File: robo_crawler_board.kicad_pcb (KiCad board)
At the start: 2 copper layers, 108.2 x 91 mm, 24 parts, among them J1 Screw_Terminal_01x02, J2 Screw_Terminal_01x02, J3 Screw_Terminal_01x02, J4 Screw_Terminal_01x02, J5 Screw_Terminal_01x02, J6 Screw_Terminal_01x02, J7 Screw_Terminal_01x02, J8 Screw_Terminal_01x02, J9 Screw_Terminal_01x02, Q1 IRLZ44N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

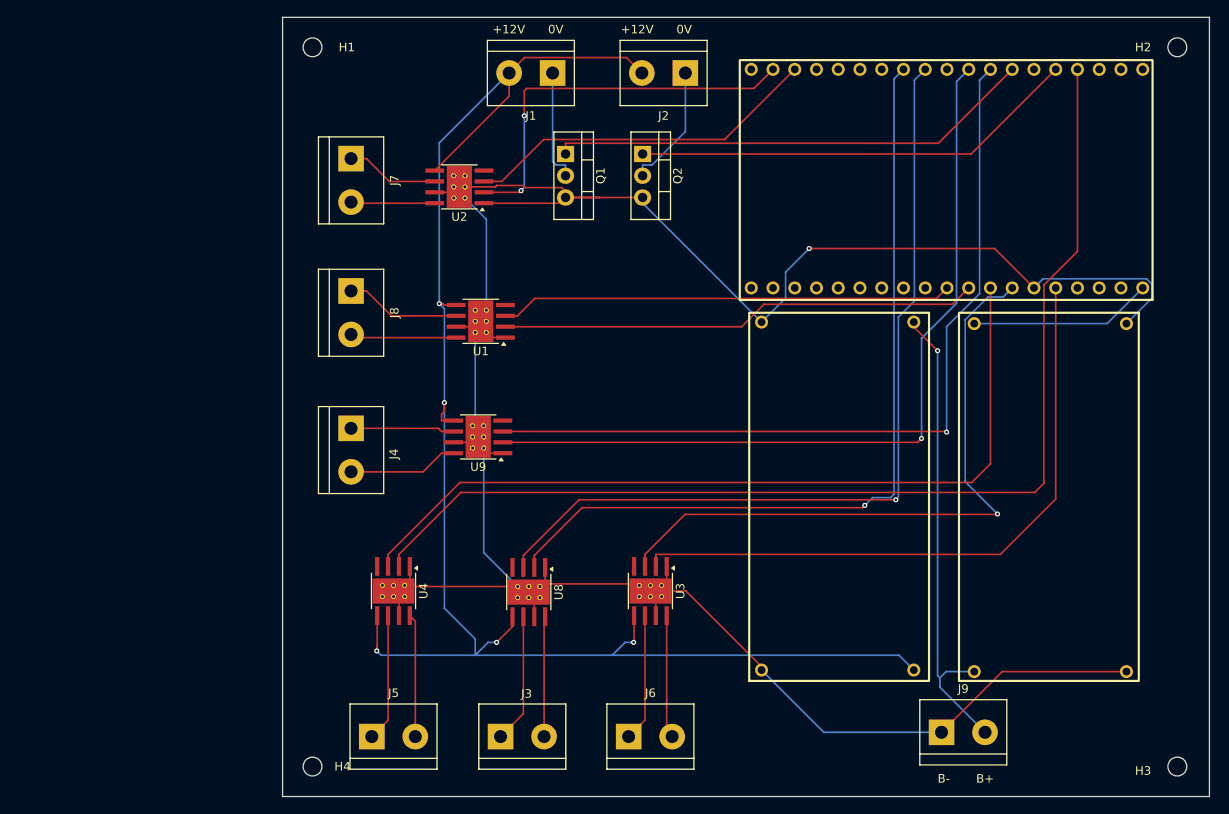
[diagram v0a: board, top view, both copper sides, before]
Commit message: adjusted for EPL manufacturing
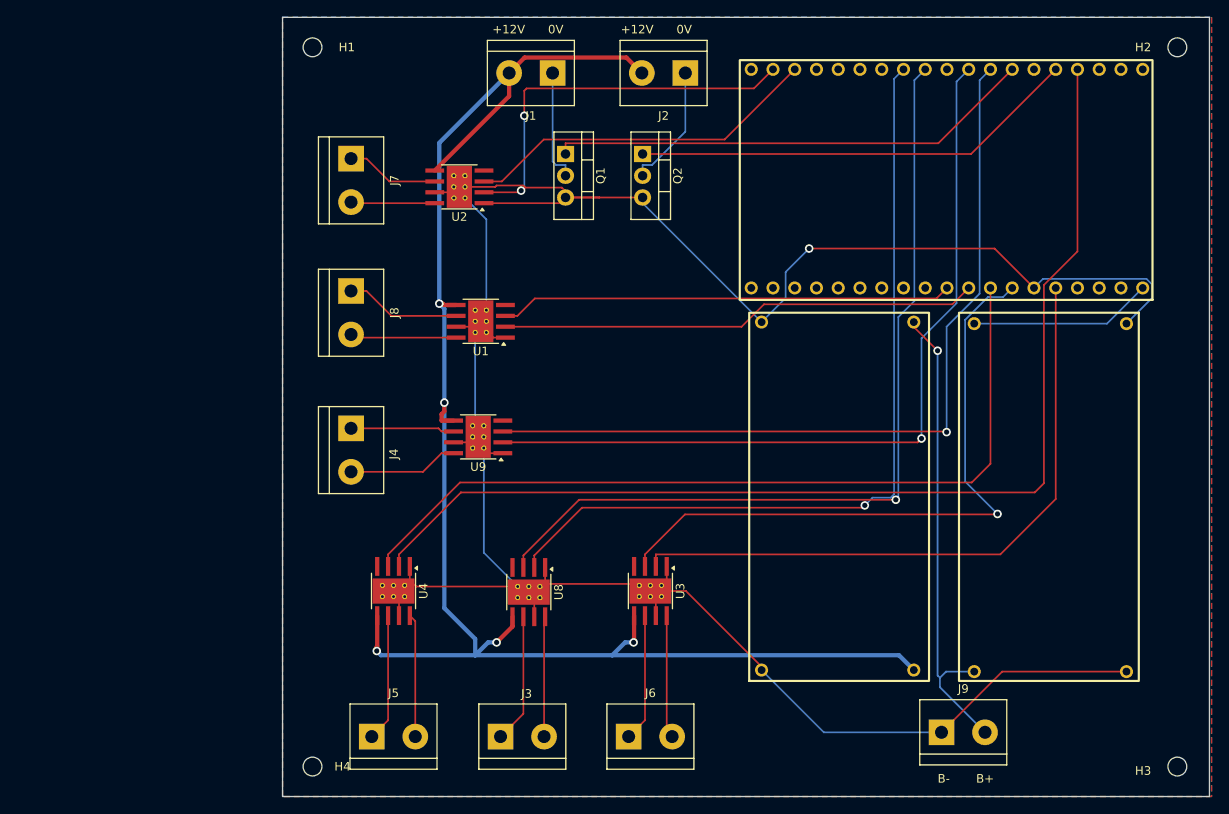
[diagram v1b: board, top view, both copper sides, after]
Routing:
- added copper zone on B.Cu, net GND
- added copper zone on F.Cu, net GND
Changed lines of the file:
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@@
 		(tenting front back)
 		(pcbplotparams
-			(layerselection 0x00000000_00000000_55555555_5755f5ff)
+			(layerselection 0x00000000_00000000_55555555_57555555)
 			(plot_on_all_layers_selection 0x00000000_00000000_00000000_00000000)
 			(disableapertmacros no)
@@
 			(outputformat 1)
 			(mirror no)
-			(drillshape 1)
+			(drillshape 0)
 			(scaleselection 1)
 			(outputdirectory "")
@@
 		(start 190.9635 125.4715)
 		(end 190.722 125.23)
-		(width 0.2)
+		(width 0.5)
 		(layer "F.Cu")
 		(net 2)
@@
 		(start 135.8968 95.0168)
 		(end 135.5733 95.3403)
-		(width 0.2)
+		(width 0.5)
 		(layer "F.Cu")
 		(net 2)
@@
 		(start 143.46 55.5)
 		(end 143.46 58.21)
-		(width 0.2)
+		(width 0.5)
 		(layer "F.Cu")
 		(net 2)
@@
 		(start 128 123)
 		(end 128 122.5)
-		(width 0.2)
+		(width 0.5)
 		(layer "F.Cu")
 		(net 2)
@@
 		(start 135.5733 95.3403)
 		(end 135.5733 96.095)
-		(width 0.2)
+		(width 0.5)
 		(layer "F.Cu")
 		(net 2)
@@
 		(start 145.2617 53.6983)
 		(end 157.1583 53.6983)
-		(width 0.2)
+		(width 0.5)
 		(layer "F.Cu")
 		(net 2)
@@
 		(start 135.3027 82.4375)
 		(end 135.7158 82.4375)
-		(width 0.2)
+		(width 0.5)
 		(layer "F.Cu")
 		(net 2)
@@
 		(start 135.5733 96.095)
 		(end 136.975 96.095)
-		(width 0.2)
+		(width 0.5)
 		(layer "F.Cu")
 		(net 2)
@@
 		(start 142 122)
 		(end 143.855 120.145)
-		(width 0.2)
+		(width 0.5)
 		(layer "F.Cu")
 		(net 2)
@@
 		(start 158.055 121.945)
 		(end 158.055 118.875)
-		(width 0.2)
+		(width 0.5)
 		(layer "F.Cu")
 		(net 2)
@@
 		(start 143.46 55.5)
 		(end 145.2617 53.6983)
-		(width 0.2)
+		(width 0.5)
 		(layer "F.Cu")
 		(net 2)
@@
 		(start 158 122)
 		(end 158.055 121.945)
-		(width 0.2)
+		(width 0.5)
 		(layer "F.Cu")
 		(net 2)
@@
 		(start 143.855 120.145)
 		(end 143.855 119)
-		(width 0.2)
+		(width 0.5)
 		(layer "F.Cu")
 		(net 2)
@@
 		(start 135.8733 82.595)
 		(end 137.275 82.595)
-		(width 0.2)
+		(width 0.5)
 		(layer "F.Cu")
 		(net 2)
@@
 		(start 128 122.5)
 		(end 128.055 122.445)
-		(width 0.2)
+		(width 0.5)
 		(layer "F.Cu")
 		(net 2)
@@
 		(start 128.055 122.445)
 		(end 128.055 118.875)
-		(width 0.2)
+		(width 0.5)
 		(layer "F.Cu")
 		(net 2)
@@
 		(start 157.1583 53.6983)
 		(end 158.96 55.5)
-		(width 0.2)
+		(width 0.5)
 		(layer "F.Cu")
 		(net 2)
@@
 		(start 143.46 58.21)
 		(end 134.775 66.895)
-		(width 0.2)
+		(width 0.5)
 		(layer "F.Cu")
 		(net 2)
@@
 		(start 135.7158 82.4375)
 		(end 135.8733 82.595)
-		(width 0.2)
+		(width 0.5)
 		(layer "F.Cu")
 		(net 2)
@@
 		(start 135.8968 94)
 		(end 135.8968 95.0168)
-		(width 0.2)
+		(width 0.5)
 		(layer "F.Cu")
 		(net 2)
@@
 	(via
 		(at 128 123)
-		(size 0.6)
-		(drill 0.3)
+		(size 1)
+		(drill 0.6)
 		(layers "F.Cu" "B.Cu")
 		(net 2)
@@
 	(via
 		(at 135.8968 94)
-		(size 0.6)
-		(drill 0.3)
+		(size 1)
+		(drill 0.6)
 		(layers "F.Cu" "B.Cu")
 		(net 2)
@@
 	(via
 		(at 142 122)
-		(size 0.6)
-		(drill 0.3)
+		(size 1)
+		(drill 0.6)
 		(layers "F.Cu" "B.Cu")
 		(net 2)
@@
 	(via
 		(at 135.3027 82.4375)
-		(size 0.6)
-		(drill 0.3)
+		(size 1)
+		(drill 0.6)
 		(layers "F.Cu" "B.Cu")
 		(net 2)
@@
 	(via
 		(at 158 122)
-		(size 0.6)
-		(drill 0.3)
+		(size 1)
+		(drill 0.6)
 		(layers "F.Cu" "B.Cu")
 		(net 2)
@@
 		(start 190.722 125.23)
 		(end 188.992 123.5)
-		(width 0.2)
+		(width 0.5)
 		(layer "B.Cu")
 		(net 2)
@@
 		(start 188.992 123.5)
 		(end 155.5 123.5)
-		(width 0.2)
+		(width 0.5)
 		(layer "B.Cu")
 		(net 2)
@@
 		(start 128.5 123.5)
 		(end 128 123)
-		(width 0.2)
+		(width 0.5)
 		(layer "B.Cu")
 		(net 2)
@@
 		(start 155.5 123.5)
 		(end 157 122)
-		(width 0.2)
+		(width 0.5)
 		(layer "B.Cu")
 		(net 2)
@@
 		(start 135.3027 82.4375)
 		(end 135.3027 63.6573)
-		(width 0.2)
+		(width 0.5)
 		(layer "B.Cu")
 		(net 2)
@@
 		(start 141 122)
 		(end 142 122)
-		(width 0.2)
+		(width 0.5)
 		(layer "B.Cu")
 		(net 2)
@@
 		(start 139.5 123.5)
 		(end 141 122)
-		(width 0.2)
+		(width 0.5)
 		(layer "B.Cu")
 		(net 2)
@@
 		(start 135.8968 94)
 		(end 135.8968 118)
-		(width 0.2)
+		(width 0.5)
 		(layer "B.Cu")
 		(net 2)
@@
 		(start 135.8968 94)
 		(end 135.8968 83.0316)
-		(width 0.2)
+		(width 0.5)
 		(layer "B.Cu")
 		(net 2)
@@
 		(start 139.5 121.6032)
 		(end 135.8968 118)
-		(width 0.2)
+		(width 0.5)
 		(layer "B.Cu")
 		(net 2)
@@
 		(start 139.5 123.5)
 		(end 128.5 123.5)
-		(width 0.2)
+		(width 0.5)
 		(layer "B.Cu")
 		(net 2)
@@
 		(start 157 122)
 		(end 158 122)
-		(width 0.2)
+		(width 0.5)
 		(layer "B.Cu")
 		(net 2)
@@
 		(start 135.3027 63.6573)
 		(end 143.46 55.5)
-		(width 0.2)
+		(width 0.5)
 		(layer "B.Cu")
 		(net 2)
@@
 		(start 135.8968 83.0316)
 		(end 135.3027 82.4375)
-		(width 0.2)
+		(width 0.5)
 		(layer "B.Cu")
 		(net 2)
@@
 		(start 155.5 123.5)
 		(end 139.5 123.5)
-		(width 0.2)
+		(width 0.5)
 		(layer "B.Cu")
 		(net 2)
@@
 		(start 139.5 123.5)
 		(end 139.5 121.6032)
-		(width 0.2)
+		(width 0.5)
 		(layer "B.Cu")
 		(net 2)
@@
 	(via
 		(at 178.5 76)
-		(size 0.6)
-		(drill 0.3)
+		(size 1)
+		(drill 0.6)
 		(layers "F.Cu" "B.Cu")
 		(net 16)
@@
 	(via
 		(at 145.2315 60.5)
-		(size 0.6)
-		(drill 0.3)
+		(size 1)
+		(drill 0.6)
 		(layers "F.Cu" "B.Cu")
 		(net 23)
@@
 	(via
 		(at 144.861 69.2384)
-		(size 0.6)
-		(drill 0.3)
+		(size 1)
+		(drill 0.6)
 		(layers "F.Cu" "B.Cu")
 		(net 23)
@@
 	(via
 		(at 200.5 107)
-		(size 0.6)
-		(drill 0.3)
+		(size 1)
+		(drill 0.6)
 		(layers "F.Cu" "B.Cu")
 		(net 27)
@@
 	(via
 		(at 188.6216 105.3433)
-		(size 0.6)
-		(drill 0.3)
+		(size 1)
+		(drill 0.6)
 		(layers "F.Cu" "B.Cu")
 		(net 36)
@@
 	(via
 		(at 185 106)
-		(size 0.6)
-		(drill 0.3)
+		(size 1)
+		(drill 0.6)
 		(layers "F.Cu" "B.Cu")
 		(net 48)
@@
 	(via
 		(at 191.6219 98.1885)
-		(size 0.6)
-		(drill 0.3)
+		(size 1)
+		(drill 0.6)
 		(layers "F.Cu" "B.Cu")
 		(net 50)
@@
 	(via
 		(at 194.5548 97.441)
-		(size 0.6)
-		(drill 0.3)
+		(size 1)
+		(drill 0.6)
 		(layers "F.Cu" "B.Cu")
 		(net 55)
@@
 	(via
 		(at 193.5 87.9351)
-		(size 0.6)
-		(drill 0.3)
+		(size 1)
+		(drill 0.6)
 		(layers "F.Cu" "B.Cu")
 		(net 60)
@@
 		(net 60)
 	)
+	(zone
+		(net 16)
+		(net_name "GND")
+		(layers "F.Cu" "B.Cu")
+		(hatch edge 0.5)
+		(connect_pads
+			(clearance 0.5)
+		)
+		(min_thickness 0.25)
+		(filled_areas_thickness no)
+		(fill yes
+			(thermal_gap 0.5)
+			(thermal_bridge_width 0.5)
+		)
+		(polygon
+			(pts
+				(xy 117 49) (xy 225.5 49) (xy 225.5 140) (xy 117 140)
+			)
+		)
+	)
 	(embedded_fonts no)

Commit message: cleaning repo
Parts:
- added R1: 15k, Resistor_SMD:R_0805_2012Metric, F.Cu at (144.1, 79.5)
- added R2: 15k, Resistor_SMD:R_0805_2012Metric, F.Cu at (141.1, 64.5)
- added R3: 15k, Resistor_SMD:R_0805_2012Metric, F.Cu at (154.9, 113.0)
- added R4: 15k, Resistor_SMD:R_0805_2012Metric, F.Cu at (124.5, 114.1)
- added R5: 15k, Resistor_SMD:R_0805_2012Metric, F.Cu at (139.9, 113.0)
- added R6: 15k, Resistor_SMD:R_0805_2012Metric, F.Cu at (142.0, 93.0)
- H1, H2, H3, H4: value M2 Size -> MountingHole
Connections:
- U1 pad 4: unconnected-(U1-ILIM-Pad4) -> Net-(U1-ILIM)
- U2 pad 4: unconnected-(U2-ILIM-Pad4) -> Net-(U2-ILIM)
- U3 pad 4: unconnected-(U3-ILIM-Pad4) -> Net-(U3-ILIM)
- U4 pad 4: unconnected-(U4-ILIM-Pad4) -> Net-(U4-ILIM)
- U8 pad 4: unconnected-(U8-ILIM-Pad4) -> Net-(U8-ILIM)
- U9 pad 4: unconnected-(U9-ILIM-Pad4) -> Net-(U9-ILIM)
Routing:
- net GND: track 316.8 -> 361.3 mm
- net +12V: track 192.1 -> 202.2 mm
- net Net-(U4-ILIM): track 0.00 -> 3.58 mm
- net Net-(U3-IN1): track 75.8 -> 72.3 mm
- net Net-(U9-ILIM): track 0.00 -> 3.17 mm
- net Net-(U1-ILIM): track 0.00 -> 3.16 mm
- net Net-(U8-ILIM): track 0.00 -> 3.13 mm
- net Net-(U2-ILIM): track 0.00 -> 2.54 mm
- net Net-(U2-IN2): track 47.4 -> 45.0 mm
- net Net-(U3-ILIM): track 0.00 -> 2.28 mm
- removed copper zone on B.Cu, net GND
- removed copper zone on F.Cu, net GND

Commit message: Reworking board design
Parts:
- removed J8, J9: Screw_Terminal_01x02, TerminalBlock:TerminalBlock_bornier-2_P5.08mm
- removed Q1, Q2: IRLZ44N, Package_TO_SOT_THT:TO-220-3_Vertical
- H1, H2, H4: footprint MountingHole:MountingHole_2.2mm_M2 -> MountingHole:MountingHole_2.2mm_M2_Pad
- H3: value MountingHole -> M2; footprint MountingHole:MountingHole_2.2mm_M2 -> MountingHole:MountingHole_2.2mm_M2_Pad
- U1: value DRV8871DDA -> ~; footprint Package_SO:Texas_HTSOP-8-1EP_3.9x4.9mm_P1.27mm_EP2.95x4.9mm_Mask2.4x3.1mm_ThermalVias -> deadzone_footprints:esp32-32u
- U2, U3: value DRV8871DDA -> ~; footprint Package_SO:Texas_HTSOP-8-1EP_3.9x4.9mm_P1.27mm_EP2.95x4.9mm_Mask2.4x3.1mm_ThermalVias -> deadzone_footprints:LM2596 DC-DC Buck Converter
- U5: value ~ -> DRV8871DDA; footprint deadzone_footprints:esp32-32u -> Package_SO:Texas_HTSOP-8-1EP_3.9x4.9mm_P1.27mm_EP2.95x4.9mm_Mask2.4x3.1mm_ThermalVias
- U6, U7: value ~ -> DRV8871DDA; footprint deadzone_footprints:LM2596 DC-DC Buck Converter -> Package_SO:Texas_HTSOP-8-1EP_3.9x4.9mm_P1.27mm_EP2.95x4.9mm_Mask2.4x3.1mm_ThermalVias
- moved U6 102.6 mm to (104.1, 99.4), turned to 180 degrees
- moved U5 91.5 mm to (103.8, 80.4)
- moved U7 82.3 mm to (100.0, 112.4), turned to 180 degrees
- moved J3 76.5 mm to (92.7, 74.9), turned to -90 degrees
- moved J2 61.5 mm to (102.5, 57.1)
- moved U4 57.2 mm to (99.8, 67.3), turned to 180 degrees
- moved J1 48.6 mm to (180.0, 92.5), turned to 90 degrees
- moved R3 41.8 mm to (116.0, 97.8), turned to 0 degrees
- moved H3 40.5 mm to (182.6, 125.0)
- moved H2 38.9 mm to (182.6, 54.5)
- moved J6 38.4 mm to (120.7, 121.9)
- moved R1 36.0 mm to (111.0, 65.2)
- moved U9 34.7 mm to (123.1, 67.7)
- moved H4 32.9 mm to (89.6, 125.0)
- moved J4 32.5 mm to (92.7, 100.3)
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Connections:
- J1 pad 2: +12V -> Net-(J1-Pin_2)
- J2 pad 2: +12V -> Net-(J2-Pin_2)
- R1 pad 1: Net-(U1-ILIM) -> Net-(U4-ILIM)
- R2 pad 1: Net-(U2-ILIM) -> Net-(U5-ILIM)
- R3 pad 1: Net-(U3-ILIM) -> Net-(U6-ILIM)
- R4 pad 1: Net-(U4-ILIM) -> Net-(U7-ILIM)
- U1 pad 1: GND -> +5V
- U1 pad 2: Net-(U1-IN2) -> unconnected-(U1-VDD33-Pad2)
- U1 pad 3: Net-(U1-IN1) -> unconnected-(U1-EN-Pad3)
- U1 pad 4: Net-(U1-ILIM) -> unconnected-(U1-VP-Pad4)
- U1 pad 5: +12V -> unconnected-(U1-VN-Pad5)
- U1 pad 6: Net-(J8-Pin_1) -> unconnected-(U1-IO34-Pad6)
- U1 pad 7: GND -> unconnected-(U1-IO35-Pad7)
- U1 pad 8: Net-(J8-Pin_2) -> unconnected-(U1-IO32-Pad8)
- U1 pad 9: GND -> unconnected-(U1-IO33-Pad9)
- U2 pad 1: GND -> Net-(J1-Pin_1)
- U2 pad 2: Net-(U2-IN2) -> Net-(J1-Pin_2)
- U2 pad 3: Net-(U2-IN1) -> GND
- U2 pad 4: Net-(U2-ILIM) -> +12V
- U3 pad 1: GND -> Net-(J1-Pin_1)
- U3 pad 2: Net-(U3-IN2) -> Net-(J1-Pin_2)
- U3 pad 3: Net-(U3-IN1) -> GND
- U3 pad 4: Net-(U3-ILIM) -> +5V
- U4 pad 2: Net-(U4-IN2) -> MOTOR1_CH2
- U4 pad 3: Net-(U4-IN1) -> MOTOR1_CH1
- U4 pad 6: Net-(J5-Pin_1) -> Net-(J2-Pin_1)
- U4 pad 8: Net-(J5-Pin_2) -> Net-(J2-Pin_2)
- U5 pad 1: +5V -> GND
- U5 pad 2: unconnected-(U5-VDD33-Pad2) -> MOTOR2_CH2
- U5 pad 3: unconnected-(U5-EN-Pad3) -> MOTOR2_CH1
- U5 pad 4: unconnected-(U5-VP-Pad4) -> Net-(U5-ILIM)
- U5 pad 5: unconnected-(U5-VN-Pad5) -> +12V
- U5 pad 6: unconnected-(U5-IO34-Pad6) -> Net-(J3-Pin_1)
- U5 pad 7: unconnected-(U5-IO35-Pad7) -> GND
- U5 pad 8: unconnected-(U5-IO32-Pad8) -> Net-(J3-Pin_2)
- U5 pad 9: unconnected-(U5-IO33-Pad9) -> GND
- U6 pad 2: /+Vin -> MOTOR3_CH2
- U6 pad 3: GND -> MOTOR3_CH1
- U6 pad 4: +5V -> Net-(U6-ILIM)
- U7 pad 2: /+Vin -> MOTOR4_CH2
- U7 pad 3: GND -> MOTOR4_CH1
- U7 pad 4: +12V -> Net-(U7-ILIM)
- U8 pad 2: Net-(U5-IO19) -> MOTOR5_CH2
- U8 pad 3: Net-(U5-IO18) -> MOTOR5_CH1
- U8 pad 6: Net-(J3-Pin_1) -> Net-(J6-Pin_1)
- U8 pad 8: Net-(J3-Pin_2) -> Net-(J6-Pin_2)
- U9 pad 2: Net-(U5-IO17) -> MOTOR6_CH2
- U9 pad 3: Net-(U5-IO16) -> MOTOR6_CH1
- U9 pad 6: Net-(J4-Pin_1) -> Net-(J7-Pin_1)
- U9 pad 8: Net-(J4-Pin_2) -> Net-(J7-Pin_2)
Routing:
- net GND: track 361.3 -> 0.00 mm, vias 1 -> 0
- net +12V: track 202.2 -> 0.00 mm, vias 5 -> 0
- net Net-(U4-IN2): track 130.1 -> 0.00 mm
- net Net-(U5-IO18): track 99.3 -> 0.00 mm, vias 1 -> 0
- net Net-(U5-IO16): track 96.8 -> 0.00 mm, vias 1 -> 0
- net Net-(U4-IN1): track 96.7 -> 0.00 mm
- net Net-(U5-IO19): track 96.1 -> 0.00 mm, vias 1 -> 0
- net Net-(U5-IO17): track 95.7 -> 0.00 mm, vias 1 -> 0
- net Net-(U3-IN2): track 75.4 -> 0.00 mm
- net Net-(U3-IN1): track 72.3 -> 0.00 mm, vias 1 -> 0
- net Net-(Q1-G): track 57.0 -> 0.00 mm
- net Net-(U1-IN2): track 56.0 -> 0.00 mm
- net /+Vin: track 55.5 -> 0.00 mm, vias 1 -> 0
- net Net-(U1-IN1): track 52.9 -> 0.00 mm
- net Net-(Q2-G): track 52.3 -> 0.00 mm
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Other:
- board outline removed
- board text removed: "+12V"
- board text removed: "0V"
- board text removed: "B+"
- board text removed: "B-"

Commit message: tentative rev2
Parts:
- H1, H2, H4: value MountingHole -> M2
- moved J5 0.58 mm to (97.8, 122.5)
- moved J6 0.58 mm to (120.7, 122.5)
- moved R1 0.56 mm to (110.5, 65.5)
- moved R3 0.29 mm to (116.0, 97.5)
- moved R2 0.24 mm to (116.0, 78.5)
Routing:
- net +12V: track 0.00 -> 135.4 mm, vias 0 -> 6
- net +5V: track 0.00 -> 117.0 mm
- net MOTOR4_CH2: track 0.00 -> 60.7 mm, vias 0 -> 1
- net GND: track 0.00 -> 59.3 mm, vias 0 -> 3
- net MOTOR5_CH2: track 0.00 -> 57.9 mm, vias 0 -> 1
- net Net-(J1-Pin_2): track 0.00 -> 57.8 mm
- net Net-(J1-Pin_1): track 0.00 -> 57.1 mm
- net MOTOR4_CH1: track 0.00 -> 53.3 mm, vias 0 -> 1
- net MOTOR5_CH1: track 0.00 -> 52.9 mm, vias 0 -> 1
- net MOTOR2_CH2: track 0.00 -> 45.7 mm, vias 0 -> 1
- net MOTOR1_CH1: track 0.00 -> 41.4 mm, vias 0 -> 1
- net MOTOR3_CH2: track 0.00 -> 40.0 mm, vias 0 -> 1
- net MOTOR2_CH1: track 0.00 -> 38.7 mm, vias 0 -> 1
- net MOTOR3_CH1: track 0.00 -> 37.0 mm, vias 0 -> 1
- net MOTOR1_CH2: track 0.00 -> 36.4 mm, vias 0 -> 1
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- added copper zone on B.Cu, net GND
- added copper zone on F.Cu, net GND
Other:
- board outline added: 100 x 77.5 mm
- board text added: "IN+"
- board text added: "IN-"
